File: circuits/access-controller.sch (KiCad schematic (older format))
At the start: 3 parts, among them J1 Conn_02x09_Odd_Even, J2 Molex_Mini-Fit_Jr_5566, U1 radio-housing-mounts

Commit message: Sent to fab.
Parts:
- removed J2: Molex_Mini-Fit_Jr_5566, Connector_Molex:Molex_Mini-Fit_Jr_5566-24A2_2x12_P4.20mm_Vertical, symbol Open_Automation:Molex_Mini-Fit_Jr_5566
- removed U1: radio-housing-mounts, Open_Automation:radio-housing-mounts, symbol Open_Automation:radio-housing-mounts
- added J1, J6: Conn_01x12, Connector_Phoenix_MC_HighVoltage:PhoenixContact_MC_1,5_12-G-5.08_1x12_P5.08mm_Horizontal, symbol Open_Automation:Conn_01x12
- added J2, J3, J4, J7, J8, J9: Conn_01x04, Connector_Phoenix_MC_HighVoltage:PhoenixContact_MC_1,5_4-G-5.08_1x04_P5.08mm_Horizontal, symbol Open_Automation:Conn_01x04
- added LS1: AI-3035, Open_Automation:AI-3035, symbol Open_Automation:AI-3035
- added R2: R_100, Resistor_SMD:R_0603_1608Metric_Pad0.98x0.95mm_HandSolder, symbol Open_Automation:R_100
- added U1: MCP23017_SS, Package_SO:SOIC-28W_7.5x17.9mm_P1.27mm, symbol Open_Automation:MCP23017_SS
- added U2: housing-mounts, Open_Automation:housing-mounts, symbol Open_Automation:housing-mounts
- renumbered J1 to J5
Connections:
- net labels added: AUX_CONTROL0, AUX_CONTROL1, AUX_OUT0, AUX_OUT1, AUX_SENSE0, AUX_SENSE1, AUX_STATE0, AUX_STATE1, EMAC_CLK_OUT, EMAC_RXD0, EMAC_RXD1, EMAC_RX_CRS_DV, EMAC_TXD0, EMAC_TXD1, EMAC_TX_EN, FOB0, FOB1, FOB_SENSE0, FOB_SENSE1, INTA, INTB, IO18, IO19, IO2, IO23, KEYPAD0, KEYPAD1, KEYPAD_SENSE0, KEYPAD_SENSE1, LOCK_CONTROL0, LOCK_CONTROL1, LOCK_OUT0, LOCK_OUT1, LOCK_SENSE0, LOCK_SENSE1, LOCK_STATE0, LOCK_STATE1, MDC, MDIO, MOTION0, MOTION1, MOTION_SENSE0, MOTION_SENSE1, PHY_PWR, POWER, PUSH0, PUSH1, PUSH_SENSE0, PUSH_SENSE1, PWR_SENSE, REG_POWER, SP1, SP2, SPEAKER, WG0_DATA0, WG0_DATA1, WG0_DATA_SENSE0, WG0_DATA_SENSE1, WG1_DATA0, WG1_DATA1, WG1_DATA_SENSE0, WG1_DATA_SENSE1
- net labels removed: AIN10, AIN9, AMBIENT_AIR_TEMP, AMBIENT_LIGHT, AUDIO_MUTE, AUDIO_STBY, BATTERY, BATTERY_VOLTAGE_SENSE, BLOWER_MOTOR, CAN_RX, CAN_TX, CURRENT_SENSE, DISPLAY_EN, DISPLAY_POWER, DRIVER_HEATED_SEAT_STATUS, DRIVER_SEAT_TEMP_CONTROL, DRIVER_SUNLOAD, FACT, IGNITION, IGNITION_SENSE, INSIDE_AIR_TEMP, INSIDE_AIR_TEMP_BLOWER, INSTRUMENT_SUPPLY_VOLTAGE_4, IO13, IO25, IO27, IO32, J1850, J1850_RX, J1850_TX, LOW_REF, MAIN_EN, MAIN_POWER, OUT11, PASSENGER_HEATED_SEAT_STATUS, PASSENGER_SEAT_TEMP_CONTROL, PASSENGER_SUNLOAD, REAR_DEFOG, SENSE1, TRIGGER1, UPPER_LEFT_AIR_TEMP, UPPER_RIGHT_AIR_TEMP, WHEEL_CONTROLS_SIGNAL
- wire segments 85 -> 195
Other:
- moved on the sheet: J5

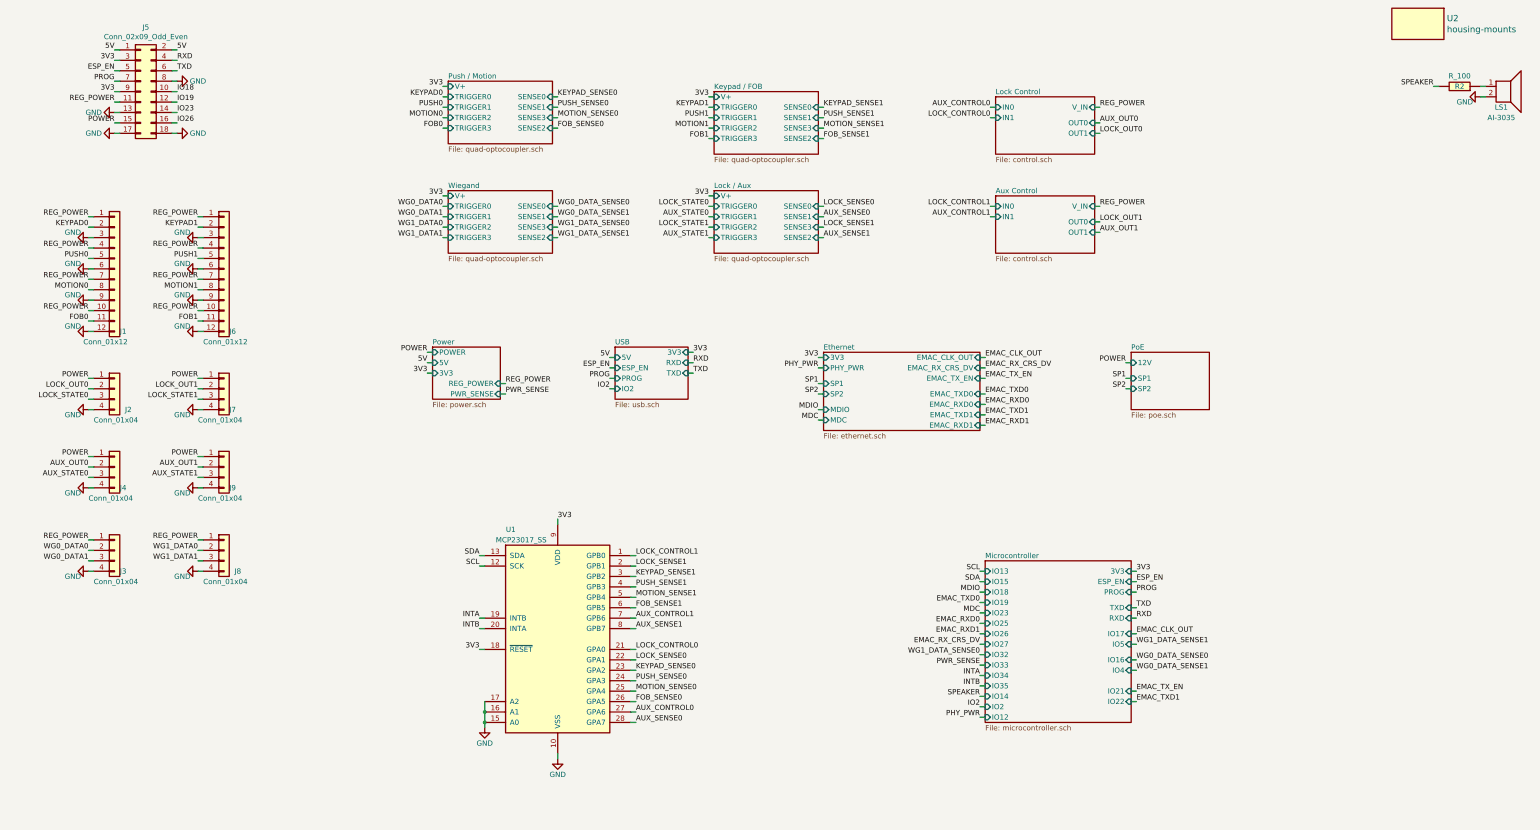
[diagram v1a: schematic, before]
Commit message: finished schematic corrections, working on layout
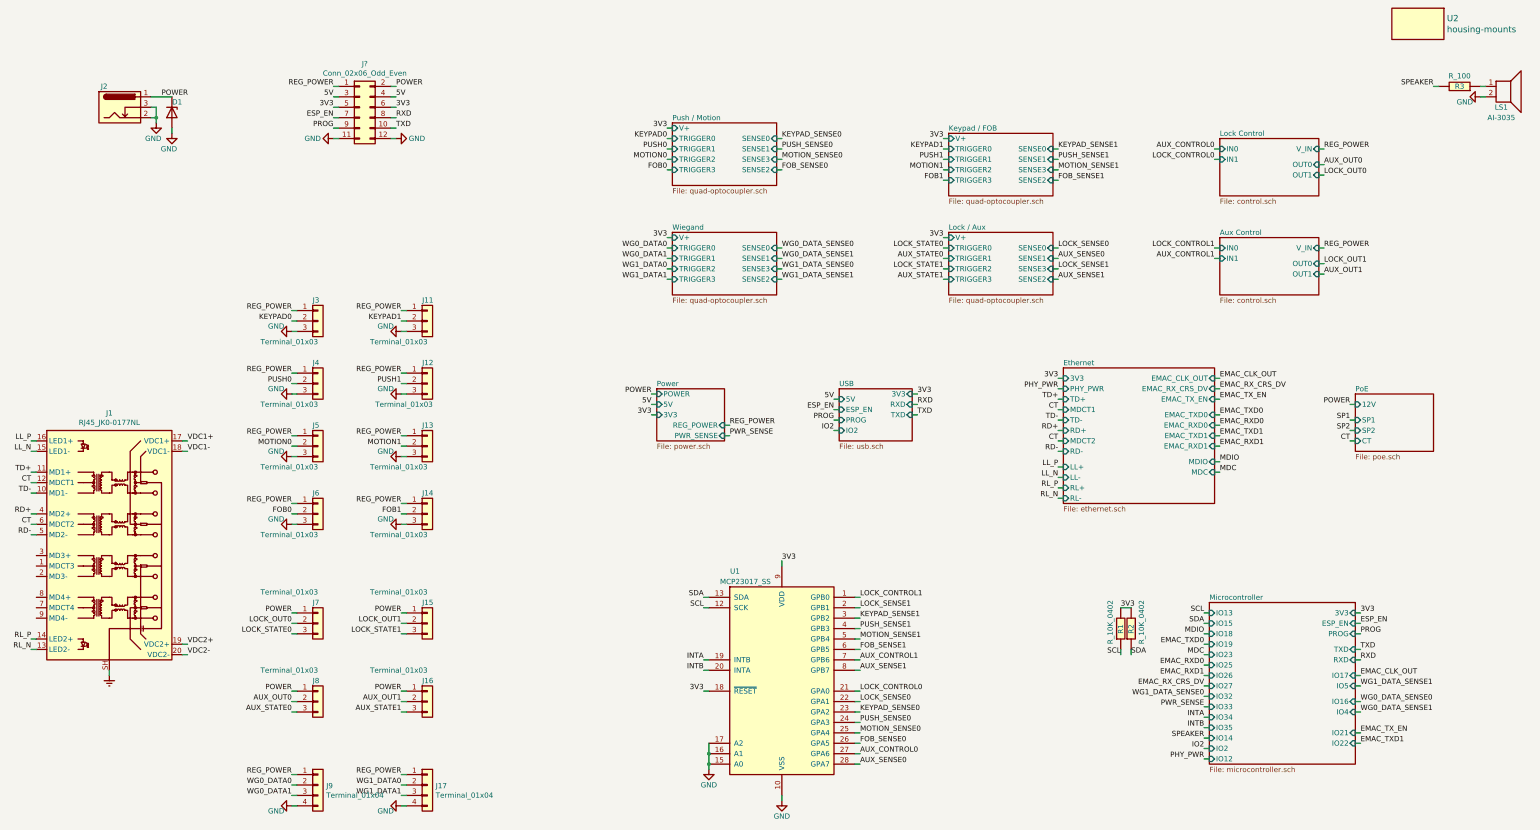
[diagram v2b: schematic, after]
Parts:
- removed J1, J6: Conn_01x12, Connector_Phoenix_MC_HighVoltage:PhoenixContact_MC_1,5_12-G-5.08_1x12_P5.08mm_Horizontal, symbol Open_Automation:Conn_01x12
- removed J2, J3, J4, J7, J8, J9: Conn_01x04, Connector_Phoenix_MC_HighVoltage:PhoenixContact_MC_1,5_4-G-5.08_1x04_P5.08mm_Horizontal, symbol Open_Automation:Conn_01x04
- removed J5: Conn_02x09_Odd_Even, Connector_PinHeader_2.54mm:PinHeader_2x09_P2.54mm_Vertical_SMD, symbol Connector_Generic:Conn_02x09_Odd_Even
- added D1: D_Zener, Diode_SMD:D_SMB_Handsoldering, symbol Open_Automation:D_Zener
- added J1: RJ45_JK0-0177NL, Open_Automation:RJ45_JK0-0177NL, symbol Open_Automation:RJ45_JK0-0177NL
- added J11, J12, J13, J14, J15, J16, J3, J4, J5, J6, J7, J8: Terminal_01x03, Open_Automation:Terminal_1,5_3-G-5.08_1x03_P5.08mm_Horizontal, symbol Open_Automation:Terminal_01x03
- added J17, J9: Terminal_01x04, Open_Automation:Terminal_1,5_4-G-5.08_1x04_P5.08mm_Horizontal, symbol Open_Automation:Terminal_01x04
- added J2: Barrel_Jack_OD5.5_ID2.5, Open_Automation:BarrelJack_OD5.5_ID2.5, symbol Open_Automation:Barrel_Jack_OD5.5_ID2.5
- added J?: Conn_02x06_Odd_Even, Connector_PinHeader_2.54mm:PinHeader_2x06_P2.54mm_Vertical_SMD, symbol Connector_Generic:Conn_02x06_Odd_Even
- added R1, R2: R_10K_0402, Resistor_SMD:R_0402_1005Metric_Pad0.72x0.64mm_HandSolder, symbol Open_Automation:R_10K_0402
- renumbered R2 to R3
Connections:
- net 3V3: now also J?.5 (Pin_5), J?.6 (Pin_6), R1.2, R2.2
- net 5V: now also J?.3 (Pin_3), J?.4 (Pin_4)
- net AUX_OUT0: now also J8.2 (Pin_2)
- net AUX_OUT1: now also J16.2 (Pin_2)
- net AUX_STATE0: now also J8.3 (Pin_3)
- net AUX_STATE1: now also J16.3 (Pin_3)
- net ESP_EN: now also J?.7 (Pin_7)
- net FOB0: now also J6.2 (Pin_2)
- net FOB1: now also J14.2 (Pin_2)
- net GND: now also D1.2 (A), J11.3 (Pin_3), J12.3 (Pin_3), J13.3 (Pin_3), J14.3 (Pin_3), J17.4 (Pin_4), J2.2, J2.3, J3.3 (Pin_3), J4.3 (Pin_3), J5.3 (Pin_3), J6.3 (Pin_3), J9.4 (Pin_4), J?.11 (Pin_11), J?.12 (Pin_12)
- net KEYPAD0: now also J3.2 (Pin_2)
- net KEYPAD1: now also J11.2 (Pin_2)
- net LOCK_OUT0: now also J7.2 (Pin_2)
- net LOCK_OUT1: now also J15.2 (Pin_2)
- net LOCK_STATE0: now also J7.3 (Pin_3)
- net LOCK_STATE1: now also J15.3 (Pin_3)
- net MOTION0: now also J5.2 (Pin_2)
- net MOTION1: now also J13.2 (Pin_2)
- net POWER: now also D1.1 (K), J15.1 (Pin_1), J16.1 (Pin_1), J2.1, J7.1 (Pin_1), J8.1 (Pin_1), J?.2 (Pin_2)
- net PROG: now also J?.9 (Pin_9)
- net PUSH0: now also J4.2 (Pin_2)
- net PUSH1: now also J12.2 (Pin_2)
- net REG_POWER: now also J11.1 (Pin_1), J12.1 (Pin_1), J13.1 (Pin_1), J14.1 (Pin_1), J17.1 (Pin_1), J3.1 (Pin_1), J4.1 (Pin_1), J5.1 (Pin_1), J6.1 (Pin_1), J9.1 (Pin_1), J?.1 (Pin_1)
- net RXD: now also J?.8 (Pin_8)
- net SCL: now also R1.1
- net SDA: now also R2.1
- net TXD: now also J?.10 (Pin_10)
- net WG0_DATA0: now also J9.2 (Pin_2)
- net WG0_DATA1: now also J9.3 (Pin_3)
- net WG1_DATA0: now also J17.2 (Pin_2)
- net WG1_DATA1: now also J17.3 (Pin_3)
- new net CT: J1.12 (MDCT1), J1.6 (MDCT2)
- new net Earth: J1.SH
- new net LL_N: J1.15 (LED1-)
- new net LL_P: J1.16 (LED1+)
- new net RD+: J1.4 (MD2+)
- new net RD-: J1.5 (MD2-)
- new net RL_N: J1.13 (LED2-)
- new net RL_P: J1.14 (LED2+)
- new net TD+: J1.11 (MD1+)
- new net TD-: J1.10 (MD1-)
- new net VDC1+: J1.17 (VDC1+)
- new net VDC1-: J1.18 (VDC1-)
- new net VDC2+: J1.19 (VDC2+)
- new net VDC2-: J1.20 (VDC2-)
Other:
- moved on the sheet: U1

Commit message: finished layout, sent to board house
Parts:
- removed U2: housing-mounts, Open_Automation:housing-mounts, symbol Open_Automation:housing-mounts
- added J20, J21, J22, J23: Conn_01x01_Female, Open_Automation:Mount_Hole, symbol Connector:Conn_01x01_Female
- gave numbers to parts that had none: 1
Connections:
- net GND: now also J20.1 (Pin_1), J21.1 (Pin_1), J22.1 (Pin_1), J23.1 (Pin_1)
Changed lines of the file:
@@
 Text Label 13700 2750 0    50   ~ 0
 REG_POWER
-$Comp
-L Open_Automation:housing-mounts U2
-U 1 1 605B420C
-P 14600 1550
-F 0 "U2" H 14878 1603 60  0000 L CNN
-F 1 "housing-mounts" H 14878 1497 60  0000 L CNN
-F 2 "Open_Automation:housing-mounts" H 14600 1600 60  0001 C CNN
-F 3 "" H 14600 1600 60  0001 C CNN
-	1    14600 1550
-	1    0    0    -1
-$EndComp
 Text Label 13700 3950 0    50   ~ 0
 AUX_OUT1
@@
 F1 "poe.sch" 50
 F2 "12V" I L 14000 5200 50
-F3 "SP1" I L 14000 5350 50
-F4 "SP2" I L 14000 5450 50
-F5 "CT" I L 14000 5550 50
+F3 "VDC1+" I R 14750 5200 50
+F4 "VDC1-" I R 14750 5300 50
+F5 "VDC2+" I R 14750 5400 50
+F6 "VDC2-" I R 14750 5500 50
 $EndSheet
 Wire Wire Line
@@
 Wire Wire Line
 	12550 8600 12600 8600
-Text Label 13950 5350 2    50   ~ 0
-SP1
-Wire Wire Line
-	13950 5350 14000 5350
-Text Label 13950 5450 2    50   ~ 0
-SP2
-Wire Wire Line
-	13950 5450 14000 5450
 Text Label 13950 5200 2    50   ~ 0
 POWER
@@
 Wire Wire Line
 	7750 7950 7800 7950
-Text Label 13950 5550 2    50   ~ 0
-CT
-Wire Wire Line
-	13950 5550 14000 5550
 $Comp
 L Open_Automation:R_10K_0402 R2
@@
 	4800 2650 4750 2650
 $Comp
-L Connector_Generic:Conn_02x06_Odd_Even J?
+L Connector_Generic:Conn_02x06_Odd_Even J10
 U 1 1 621F037F
 P 4450 2350
-F 0 "J?" H 4500 2767 50  0000 C CNN
+F 0 "J10" H 4500 2767 50  0000 C CNN
 F 1 "Conn_02x06_Odd_Even" H 4500 2676 50  0000 C CNN
 F 2 "Connector_PinHeader_2.54mm:PinHeader_2x06_P2.54mm_Vertical_SMD" H 4450 2350 50  0001 C CNN
@@
 	1    0    0    -1
 $EndComp
+Text Label 14800 5300 0    50   ~ 0
+VDC1-
+Text Label 14800 5200 0    50   ~ 0
+VDC1+
+Text Label 14800 5400 0    50   ~ 0
+VDC2+
+Text Label 14800 5500 0    50   ~ 0
+VDC2-
+Wire Wire Line
+	14750 5200 14800 5200
+Wire Wire Line
+	14800 5300 14750 5300
+Wire Wire Line
+	14800 5400 14750 5400
+Wire Wire Line
+	14750 5500 14800 5500
+$Comp
+L Connector:Conn_01x01_Female J20
+U 1 1 62533331
+P 1350 800
+F 0 "J20" H 1378 826 50  0000 L CNN
+F 1 "Conn_01x01_Female" H 1378 735 50  0000 L CNN
+F 2 "Open_Automation:Mount_Hole" H 1378 689 50  0001 L CNN
+F 3 "~" H 1350 800 50  0001 C CNN
+	1    1350 800
+	1    0    0    -1
+$EndComp
+$Comp
+L Connector:Conn_01x01_Female J21
+U 1 1 6253A5DC
+P 1350 1000
+F 0 "J21" H 1378 1026 50  0000 L CNN
+F 1 "Conn_01x01_Female" H 1378 935 50  0000 L CNN
+F 2 "Open_Automation:Mount_Hole" H 1378 889 50  0001 L CNN
+F 3 "~" H 1350 1000 50  0001 C CNN
+	1    1350 1000
+	1    0    0    -1
+$EndComp
+$Comp
+L Connector:Conn_01x01_Female J22
+U 1 1 62555B84
+P 1350 1200
+F 0 "J22" H 1378 1226 50  0000 L CNN
+F 1 "Conn_01x01_Female" H 1378 1135 50  0000 L CNN
+F 2 "Open_Automation:Mount_Hole" H 1378 1089 50  0001 L CNN
+F 3 "~" H 1350 1200 50  0001 C CNN
+	1    1350 1200
+	1    0    0    -1
+$EndComp
+$Comp
+L Connector:Conn_01x01_Female J23
+U 1 1 62555BDC
+P 1350 1400
+F 0 "J23" H 1378 1426 50  0000 L CNN
+F 1 "Conn_01x01_Female" H 1378 1335 50  0000 L CNN
+F 2 "Open_Automation:Mount_Hole" H 1378 1289 50  0001 L CNN
+F 3 "~" H 1350 1400 50  0001 C CNN
+	1    1350 1400
+	1    0    0    -1
+$EndComp
+$Comp
+L power:GND #PWR?
+U 1 1 625E6B73
+P 1100 1450
+AR Path="/5A7BADB8/625E6B73" Ref="#PWR?"  Part="1"
+AR Path="/6045445B/625E6B73" Ref="#PWR?"  Part="1"
+AR Path="/625E6B73" Ref="#PWR0105"  Part="1"
+F 0 "#PWR0105" H 1100 1200 50  0001 C CNN
+F 1 "GND" H 1150 1300 50  0000 R CNN
+F 2 "" H 1100 1450 50  0001 C CNN
+F 3 "" H 1100 1450 50  0001 C CNN
+	1    1100 1450
+	1    0    0    -1
+$EndComp
+Wire Wire Line
+	1100 1450 1100 1400
+Wire Wire Line
+	1100 1400 1150 1400
+Wire Wire Line
+	1150 800  1100 800
+Wire Wire Line
+	1100 800  1100 1000
+Connection ~ 1100 1400
+Wire Wire Line
+	1150 1200 1100 1200
+Connection ~ 1100 1200
+Wire Wire Line
+	1100 1200 1100 1400
+Wire Wire Line
+	1150 1000 1100 1000
+Connection ~ 1100 1000
+Wire Wire Line
+	1100 1000 1100 1200
 $EndSCHEMATC
